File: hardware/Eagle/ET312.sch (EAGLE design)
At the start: 48 parts, among them IC1 LM358N, J2 JTAG, Q1 2N3906, Q2 2N3904, SW2 Menu, SW4 Up, U1 MEGA16-P, U2 LM324N, U3 4066BE, U8 LTC1661CN8

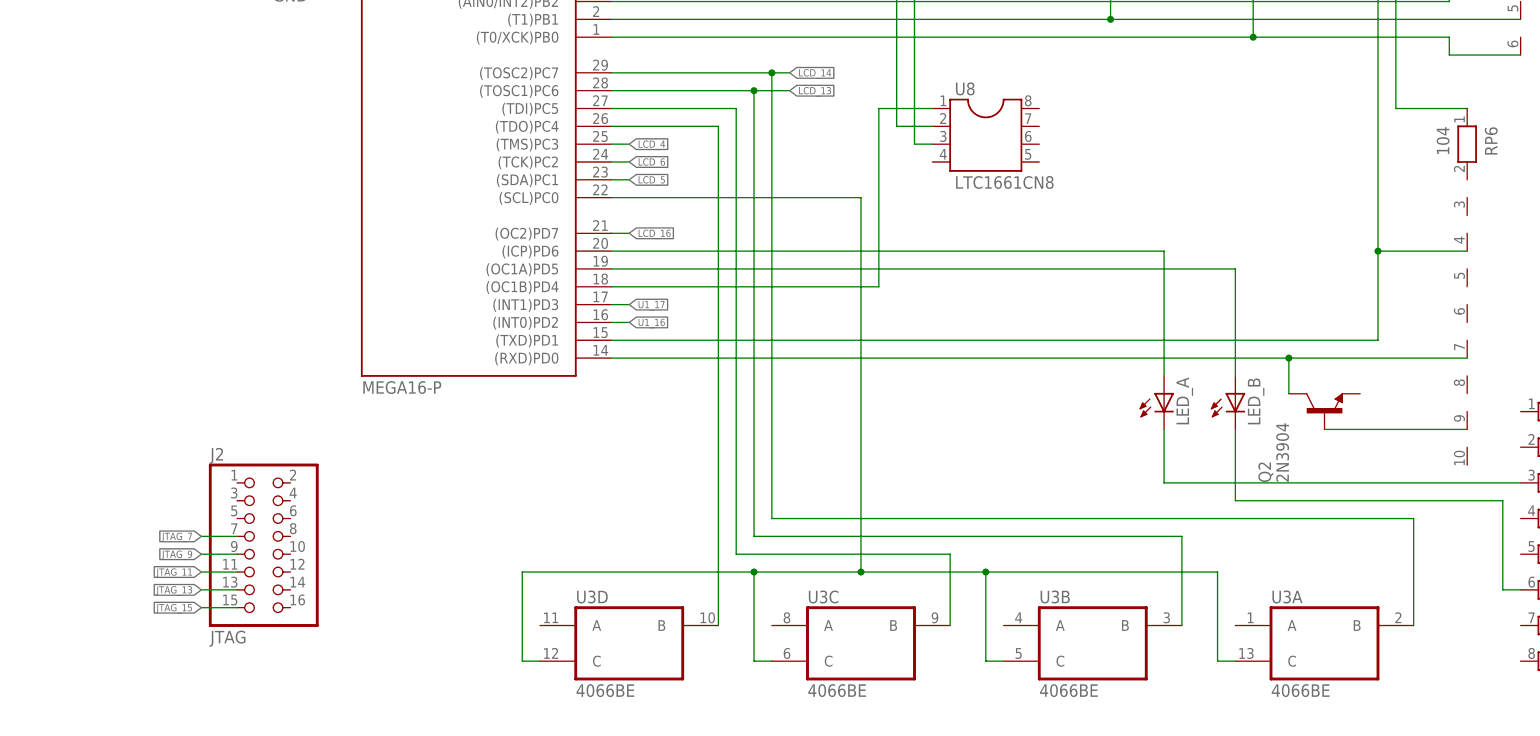
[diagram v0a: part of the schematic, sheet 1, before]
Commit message: added much of the wirings to the txt file
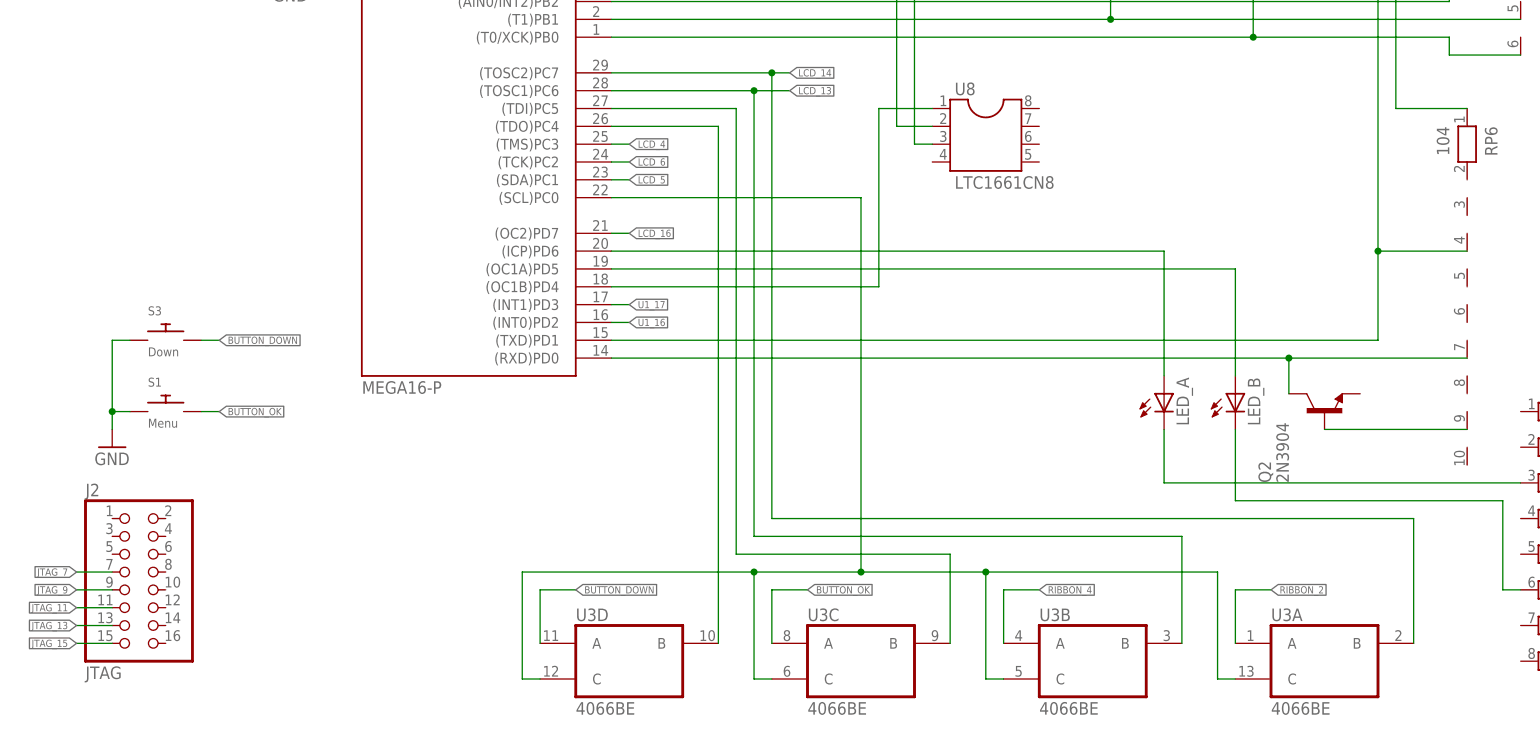
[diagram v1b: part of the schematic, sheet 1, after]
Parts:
- added S1: Menu, adafruit:SWITCH_PUSHBUTTONEVQ-PE
- added S3: Down, adafruit:SWITCH_PUSHBUTTONEVQ-PE
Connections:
- removed net N$12: U1.(SCL)PC0, U3A.C, U3B.C, U3C.C, U3D.C
- new net BUTTON_DOWN: S3.P$2, U3D.A
- new net BUTTON_OK: S1.P$2, U3C.A
- net GND: now also S1.P$1, S3.P$1
- net N$13: now also U3D.B
- net RIBBON_2: now also U3A.A
- net RIBBON_4: now also U1.(SCL)PC0, U3A.C, U3B.A, U3B.C, U3C.C, U3D.C
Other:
- moved on the sheet: J2, U3A, U3B, U3C, U3D
